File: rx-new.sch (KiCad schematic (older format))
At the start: 70 parts

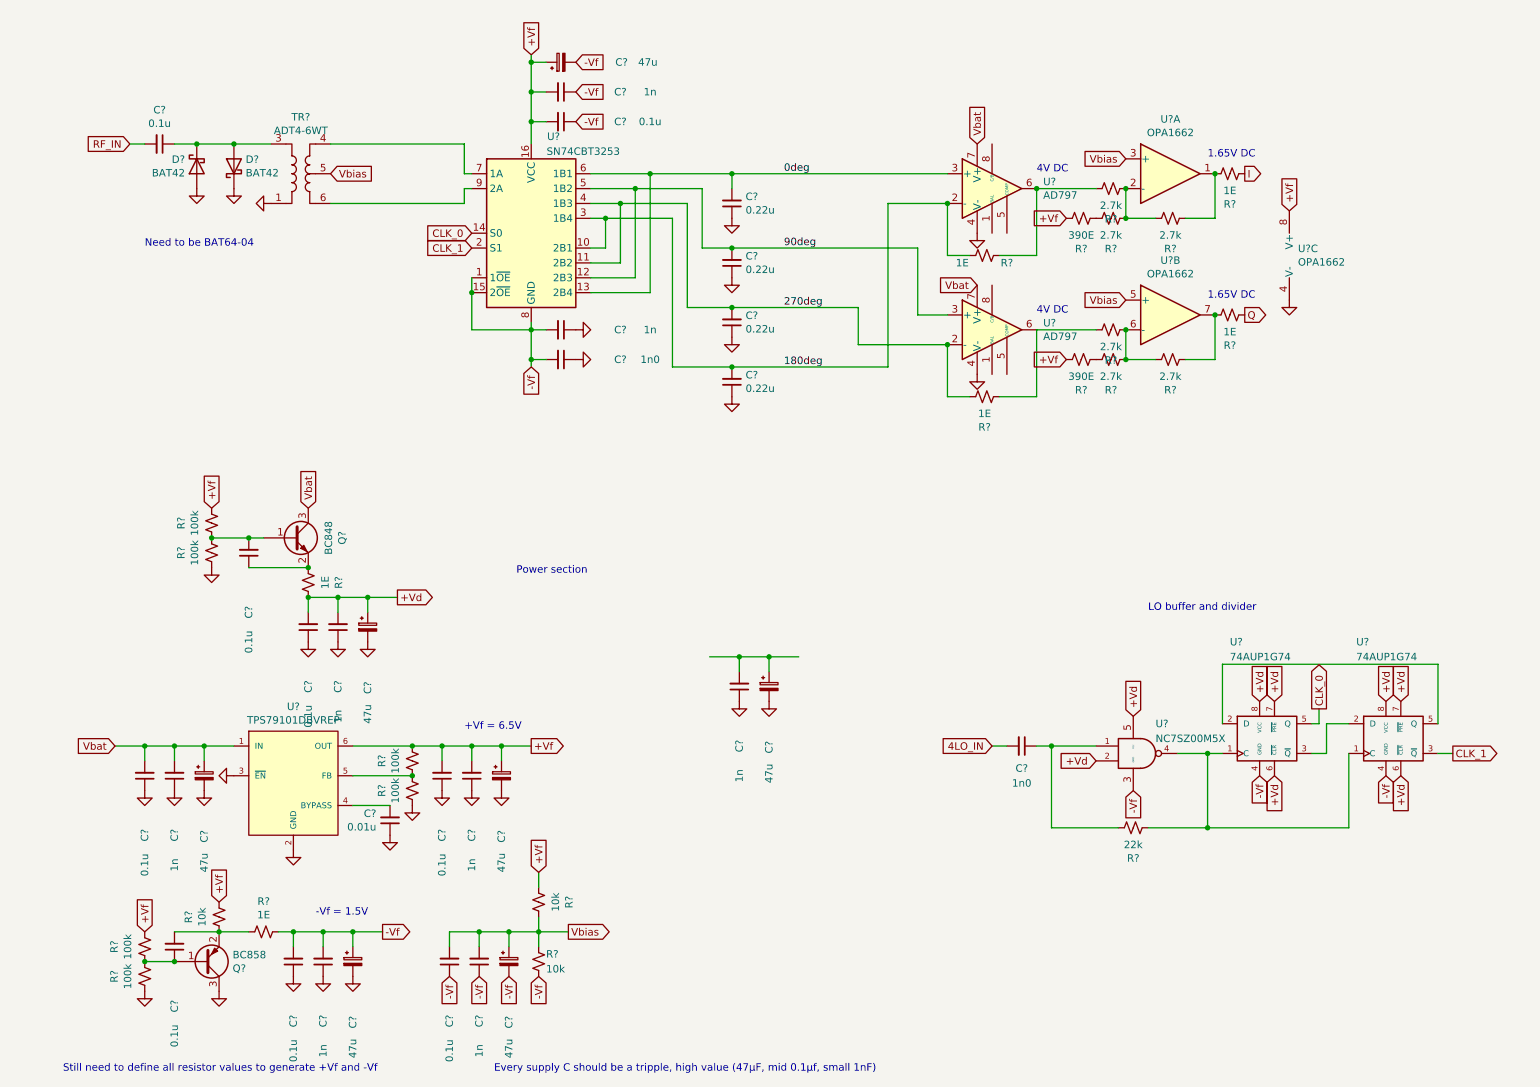
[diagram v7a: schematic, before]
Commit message: Converted labels to local labels, added supply capacitors and annotated components
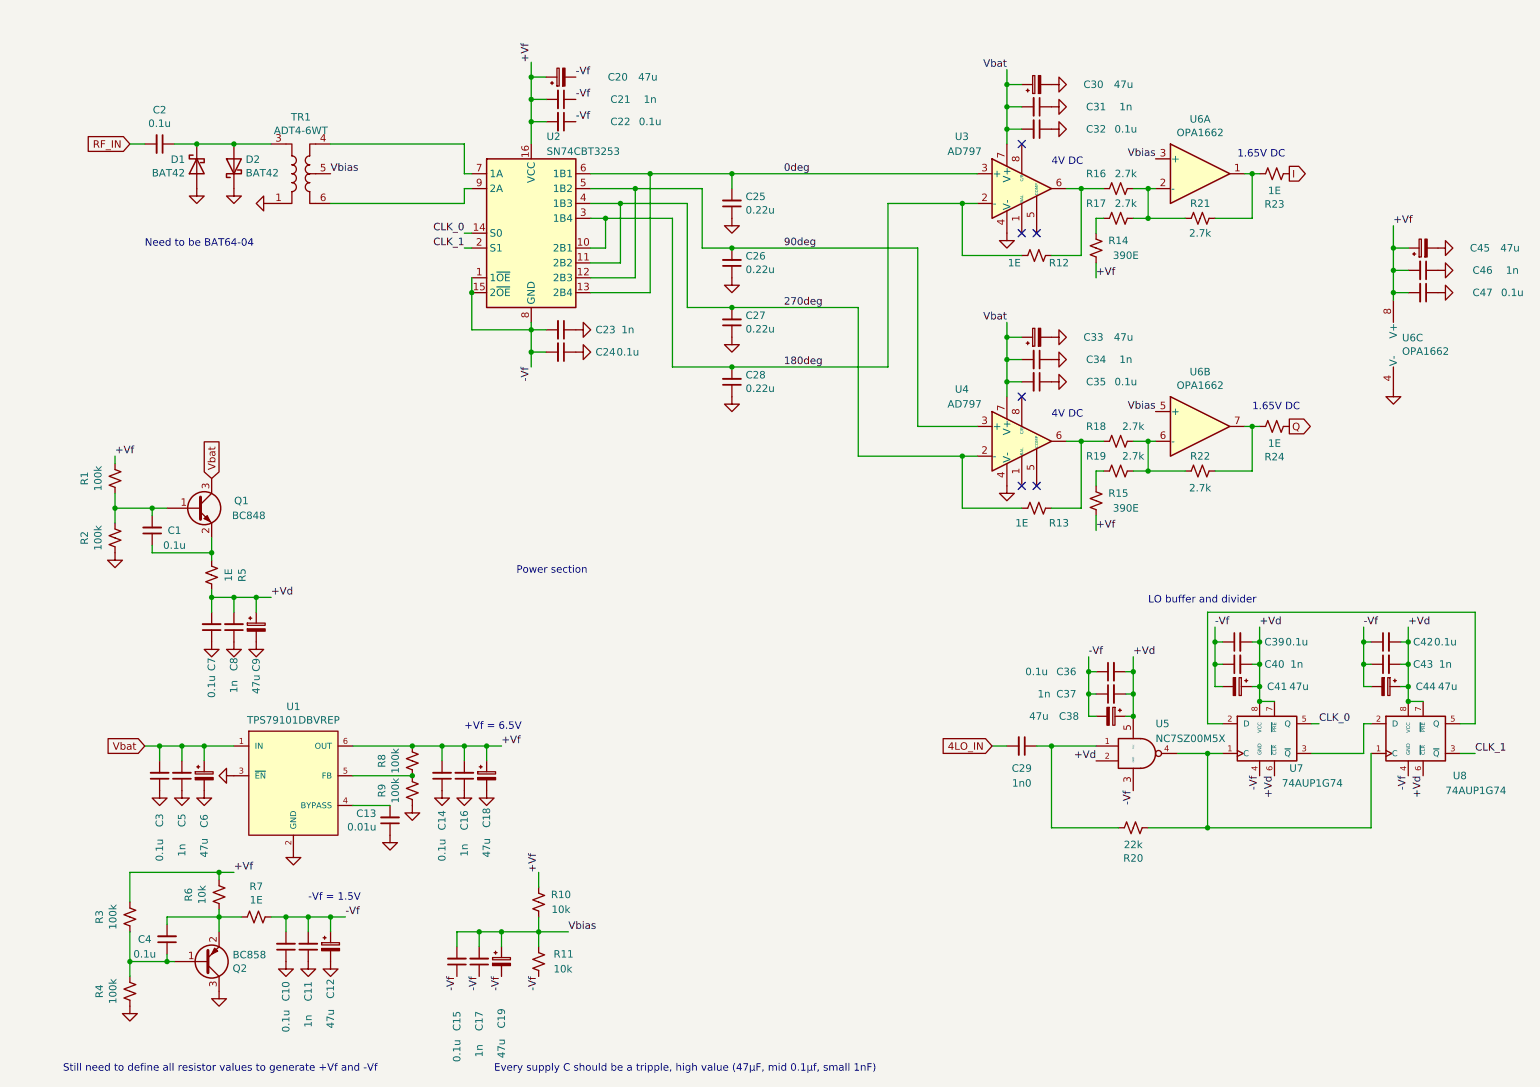
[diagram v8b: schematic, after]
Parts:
- removed C?: 47u, symbol Device:CP_Small
- removed C?: 1n, symbol Device:C_Small
- removed R?: 390E, symbol Device:R_Small_US
- added C30, C33, C38, C41, C44, C45: 47u, symbol Device:CP_Small
- added C31, C34, C37, C40, C43, C46: 1n, symbol Device:C_Small
- added C32, C35, C36, C39, C42, C47: 0.1u, symbol Device:C_Small
- added R15: 390E, symbol Device:R_Small_US
- C24: renamed from C?; value 1n0 -> 0.1u
- gave numbers to parts that had none: 64
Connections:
- net +Vd: now also C36.2, C37.2, C38.1, C39.2, C40.2, C41.1, C42.2, C43.2, C44.1
- net +Vf: now also C45.1, C46.2, C47.2, R15.1
- net -Vf: now also C36.1, C37.1, C38.2, C39.1, C40.1, C41.2, C42.1, C43.1, C44.2
- net GND: now also C30.2, C31.1, C32.1, C33.2, C34.1, C35.1, C45.2, C46.1, C47.1
- net Vbat: now also C30.1, C31.2, C32.2, C33.1, C34.2, C35.2
- net at R19.1: now also R15.2
- no-connect marks 0 -> 6
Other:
- moved on the sheet: C1, C10, C11, C12, C15, C16, C18, C19, C20, C21, C24, C3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
